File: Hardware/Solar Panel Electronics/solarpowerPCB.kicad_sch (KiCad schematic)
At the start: 38 parts, among them J3 Conn_01x02_Male, J4 Conn_01x06_Male, J5 Conn_01x02_Male, Q1 MMDT2222A, U1 SN65HVD230, U2 ESP32-PICO-D4

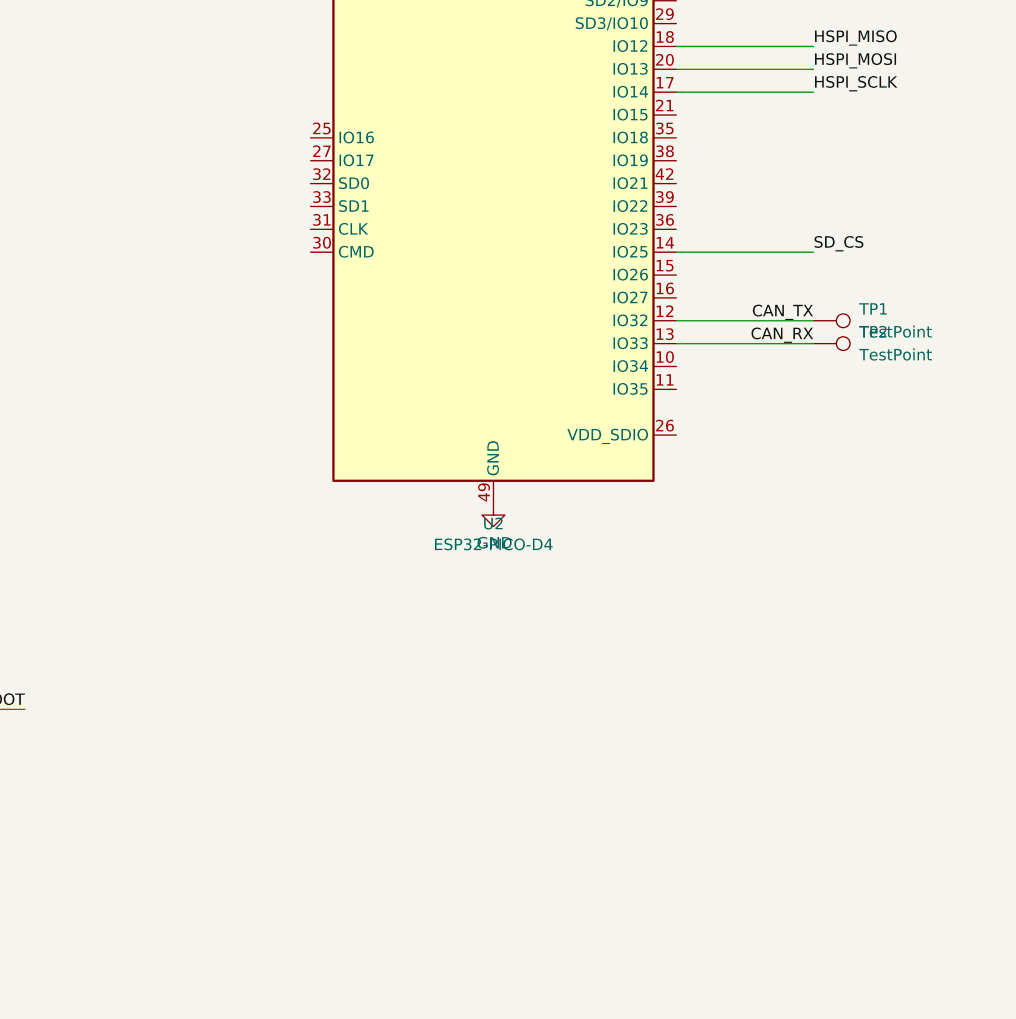
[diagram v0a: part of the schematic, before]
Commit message: Add i2c breakout
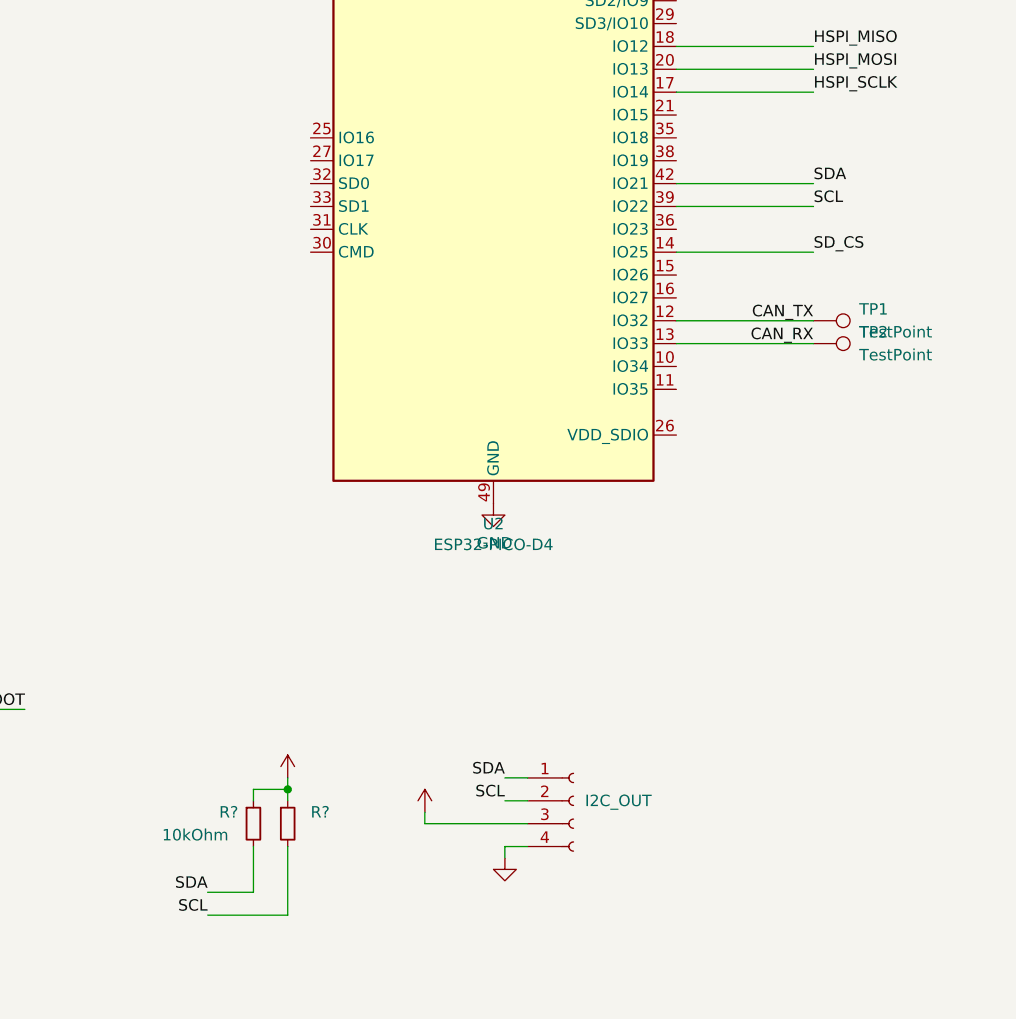
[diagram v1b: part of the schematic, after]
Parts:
- added I2C_OUT: (no value), symbol Connector:Conn_01x04_Female
- added R?: 10kOhm, symbol Device:R_Small
- added R?: (no value), symbol Device:R_Small
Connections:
- net +3V3: now also I2C_OUT.3 (Pin_3), R?.1, R?.1
- net GND: now also I2C_OUT.4 (Pin_4)
- net SCL: now reaches U2.39 (IO22)
- net SCL: now also I2C_OUT.2 (Pin_2), R?.2
- net SDA: now reaches U2.42 (IO21)
- net SDA: now also I2C_OUT.1 (Pin_1), R?.2

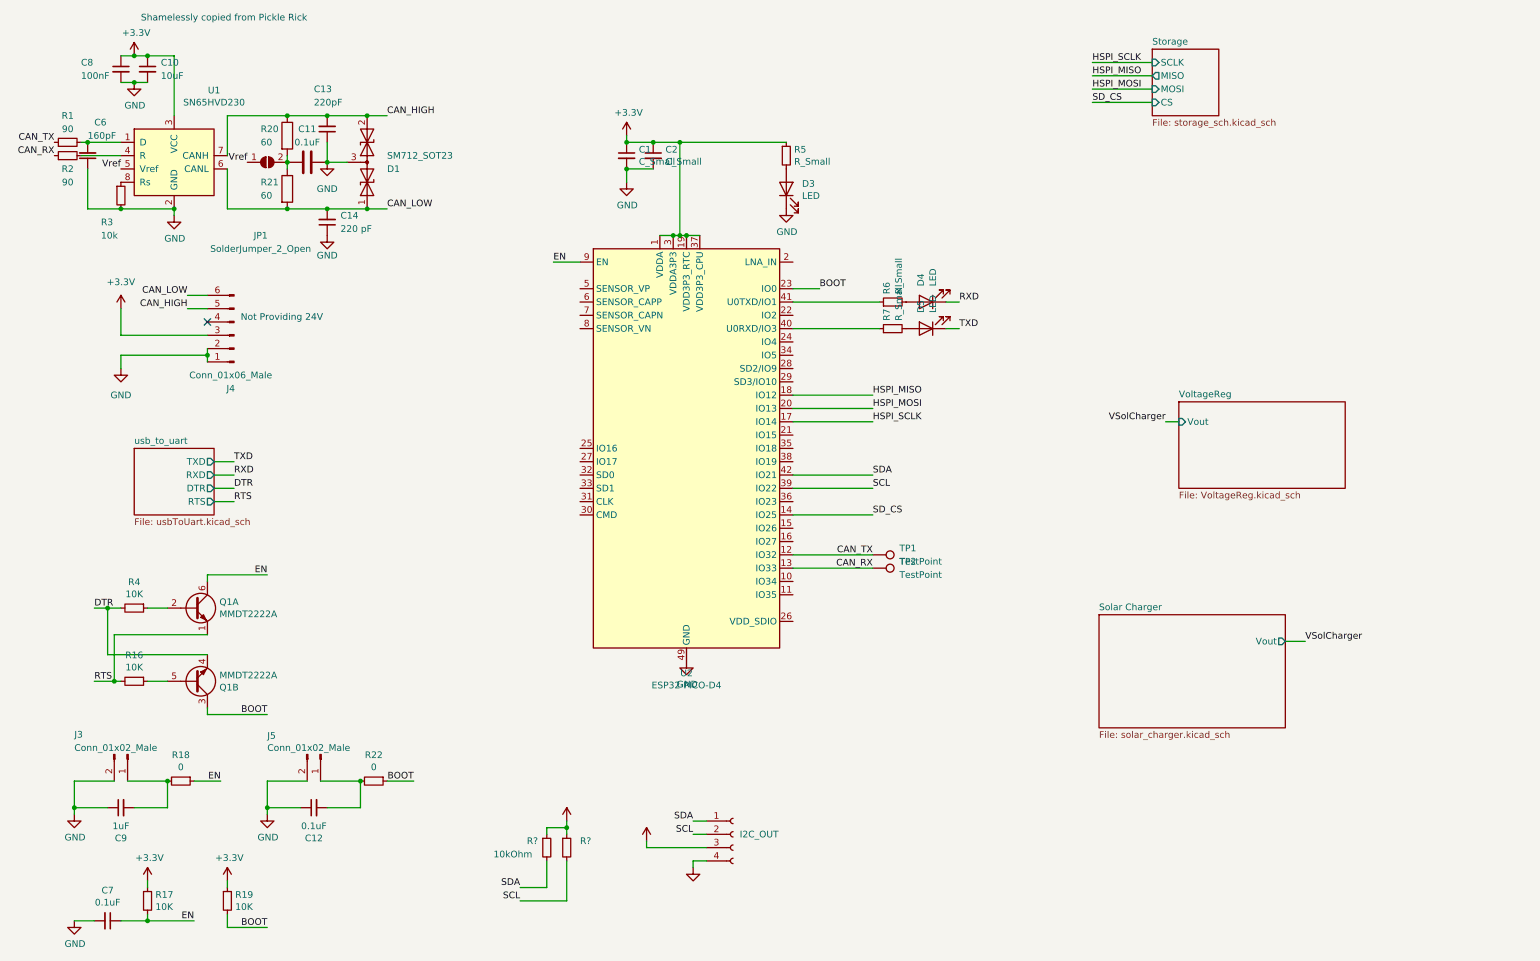
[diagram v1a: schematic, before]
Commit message: Add ADC for solar yarn patch
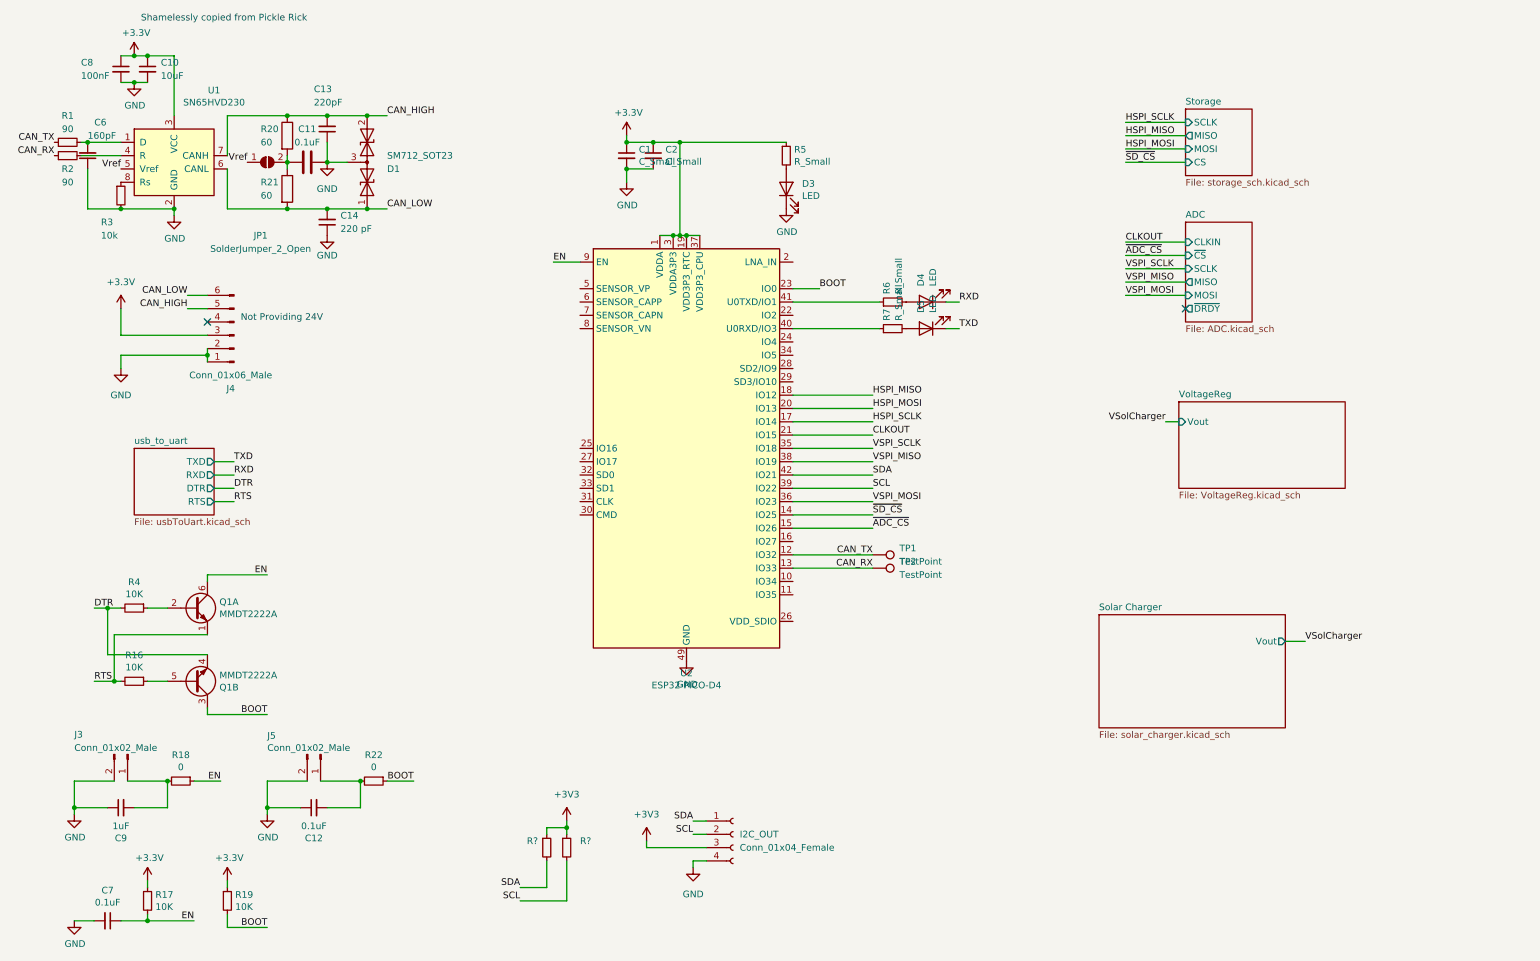
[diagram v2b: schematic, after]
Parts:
- I2C_OUT: value (none) -> Conn_01x04_Female
- R?: value 10kOhm -> (none)
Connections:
- net ~{ADC_CS}: now reaches U2.15 (IO26)
- net CLKOUT: now reaches U2.21 (IO15)
- net VSPI_SCLK: now reaches U2.35 (IO18)
- net VSPI_MOSI: now reaches U2.36 (IO23)
- net VSPI_MISO: now reaches U2.38 (IO19)
- net SD_CS renamed ~{SD_CS}
- no-connect marks 1 -> 2
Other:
- added sheet ADC (ADC.kicad_sch)

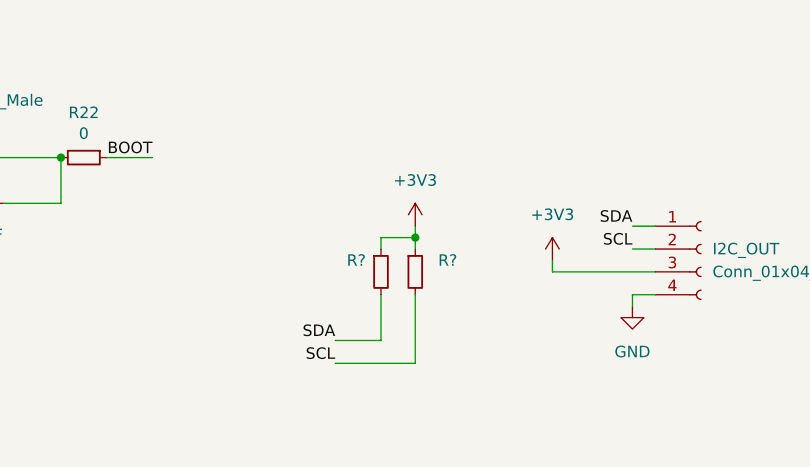
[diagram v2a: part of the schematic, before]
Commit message: Made changes to solar charging circuit
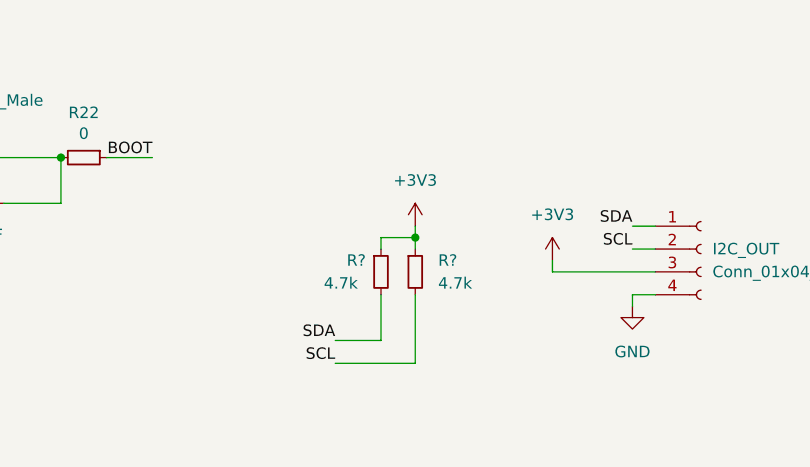
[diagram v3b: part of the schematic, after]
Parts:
- R? (x2): value (none) -> 4.7k
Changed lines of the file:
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@@
       (effects (font (size 1.27 1.27)) (justify left))
     )
-    (property "Value" "" (id 1) (at 107.95 175.26 0)
+    (property "Value" "4.7k" (id 1) (at 107.95 175.26 0)
       (effects (font (size 1.27 1.27)) (justify left))
     )
@@
       (effects (font (size 1.27 1.27)) (justify left))
     )
-    (property "Value" "" (id 1) (at 120.65 175.2599 0)
+    (property "Value" "4.7k" (id 1) (at 120.65 175.2599 0)
       (effects (font (size 1.27 1.27)) (justify left))
     )
@@
       (reference "#PWR0150") (unit 1) (value "GND") (footprint "")
     )
+    (path "/00000000-0000-0000-0000-0000624b2440/16846add-8613-4d5b-80f8-47bb821442f4"
+      (reference "#PWR?") (unit 1) (value "GND") (footprint "")
+    )
+    (path "/00000000-0000-0000-0000-0000624b2440/2139c0d5-fd19-4edc-98d3-72c046a88978"
+      (reference "#PWR?") (unit 1) (value "GND") (footprint "")
+    )
     (path "/b081b074-3171-4535-9bf1-f0e71da78e2a/2486d1b0-d5d1-4e35-85d8-e13a0287ad93"
       (reference "#PWR?") (unit 1) (value "~") (footprint "")
     )
+    (path "/00000000-0000-0000-0000-0000624b2440/31eff159-32a2-408b-bbd4-e68aecc2eed2"
+      (reference "#PWR?") (unit 1) (value "GND") (footprint "")
+    )
     (path "/b081b074-3171-4535-9bf1-f0e71da78e2a/46479943-c593-4529-bc99-371d4cd18e4c"
       (reference "#PWR?") (unit 1) (value "+3.3V") (footprint "")
@@
       (reference "#PWR?") (unit 1) (value "~") (footprint "")
     )
+    (path "/00000000-0000-0000-0000-0000624b2440/56d5a663-a675-43d4-9149-36082330973d"
+      (reference "#PWR?") (unit 1) (value "GND") (footprint "")
+    )
     (path "/bc16b27f-da78-4399-84ff-d0e67df4623d/756c57ca-b724-416e-bbc3-080fcadffb70"
       (reference "#PWR?") (unit 1) (value "GND") (footprint "")
@@
       (reference "#PWR?") (unit 1) (value "GND") (footprint "")
     )
+    (path "/00000000-0000-0000-0000-0000624b2440/9656bcd2-551d-4721-9723-a3556e1de2b8"
+      (reference "#PWR?") (unit 1) (value "GND") (footprint "")
+    )
     (path "/a5d81433-1591-493c-9981-6bad61f721d4"
       (reference "#PWR?") (unit 1) (value "GND") (footprint "")
@@
     )
     (path "/00000000-0000-0000-0000-0000624b2440/00000000-0000-0000-0000-000062475c18"
-      (reference "D7") (unit 1) (value "LED") (footprint "")
+      (reference "D7") (unit 1) (value "FAULT LED") (footprint "")
     )
     (path "/00000000-0000-0000-0000-0000624b2440/00000000-0000-0000-0000-000062477796"
-      (reference "D8") (unit 1) (value "LED") (footprint "")
+      (reference "D8") (unit 1) (value "CHRG LED") (footprint "")
     )
     (path "/00000000-0000-0000-0000-0000624b2440/00000000-0000-0000-0000-0000624944cc"
@@
       (reference "J1") (unit 1) (value "Screw_Terminal_SolarPanel_Input") (footprint "")
     )
-    (path "/00000000-0000-0000-0000-0000624b2440/00000000-0000-0000-0000-00006249cbeb"
-      (reference "J2") (unit 1) (value "Screw_Terminal_Battery") (footprint "")
-    )
     (path "/281488e8-d376-4880-a2b5-28296fef7666"
       (reference "J3") (unit 1) (value "Conn_01x02_Male") (footprint "Connector_PinHeader_2.54mm:PinHeader_1x02_P2.54mm_Vertical")
@@
       (reference "J7") (unit 1) (value "~") (footprint "")
     )
+    (path "/00000000-0000-0000-0000-0000624b2440/13dd92b6-06ca-4e0b-9ee3-12c7f508706e"
+      (reference "J?") (unit 1) (value "Screw_Terminal_SolarPanel_Input") (footprint "")
+    )
+    (path "/00000000-0000-0000-0000-0000624b2440/357ce087-9bb2-449e-8dc8-378603d15219"
+      (reference "J?") (unit 1) (value "Screw_Terminal_SolarPanel_Input") (footprint "")
+    )
+    (path "/00000000-0000-0000-0000-0000624b2440/3e1b740f-8858-4a54-b870-20ebb9090e12"
+      (reference "J?") (unit 1) (value "Screw_Terminal_SolarPanel_Input") (footprint "")
+    )
+    (path "/00000000-0000-0000-0000-0000624b2440/6cdc5bbd-bc8d-46ac-a385-b458b224ce28"
+      (reference "J?") (unit 1) (value "Conn_01x02_Male") (footprint "")
+    )
+    (path "/00000000-0000-0000-0000-0000624b2440/752b3695-5f89-4c59-a33a-3588ae69b756"
+      (reference "J?") (unit 1) (value "Screw_Terminal_SolarPanel_Input") (footprint "")
+    )
+    (path "/00000000-0000-0000-0000-0000624b2440/88ab8186-6b6a-48ca-8429-2e699b219df1"
+      (reference "J?") (unit 1) (value "Battery Connector") (footprint "Connector_JST:JST_ACH_BM02B-ACHSS-GAN-ETF_1x02-1MP_P1.20mm_Vertical")
+    )
+    (path "/00000000-0000-0000-0000-0000624b2440/bb6c885b-4252-4449-bc79-7ef98520d17d"
+      (reference "J?") (unit 1) (value "Screw_Terminal_SolarPanel_Input") (footprint "")
+    )
     (path "/b081b074-3171-4535-9bf1-f0e71da78e2a/fc728988-eca1-4a8e-8ed8-022e113a9c98"
       (reference "J?") (unit 1) (value "~") (footprint "")
@@
       (reference "R11") (unit 1) (value "10k") (footprint "")
     )
-    (path "/00000000-0000-0000-0000-0000624b2440/00000000-0000-0000-0000-0000624843bf"
-      (reference "R12") (unit 1) (value "NXFT15XH103FA1B110") (footprint "Murata_Electronics_North_America-NXF_151B110-0-0-*")
-    )
     (path "/00000000-0000-0000-0000-0000624b2440/00000000-0000-0000-0000-00006247f44b"
       (reference "R13") (unit 1) (value "560k") (footprint "")
@@
       (reference "TP5") (unit 1) (value "TestPoint") (footprint "TestPoint:TestPoint_Pad_D1.0mm")
     )
+    (path "/00000000-0000-0000-0000-0000624b2440/89425070-2cf4-40a0-b141-4db438b807a5"
+      (reference "TP?") (unit 1) (value "TP_BAT") (footprint "")
+    )
+    (path "/00000000-0000-0000-0000-0000624b2440/a6e67203-b292-4b44-a752-28ae4206406d"
+      (reference "TP?") (unit 1) (value "TP_Vout") (footprint "")
+    )
+    (path "/00000000-0000-0000-0000-0000624b2440/b5071fcf-b3e7-4725-a3db-bca61fd551be"
+      (reference "TP?") (unit 1) (value "TP_Vsolarpanel") (footprint "")
+    )
     (path "/c025e6d2-e820-404e-abc2-337eef32c295"
